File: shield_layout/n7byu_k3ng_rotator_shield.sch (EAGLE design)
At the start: 22 parts, among them J1 ARDUINO_R3_SHIELD

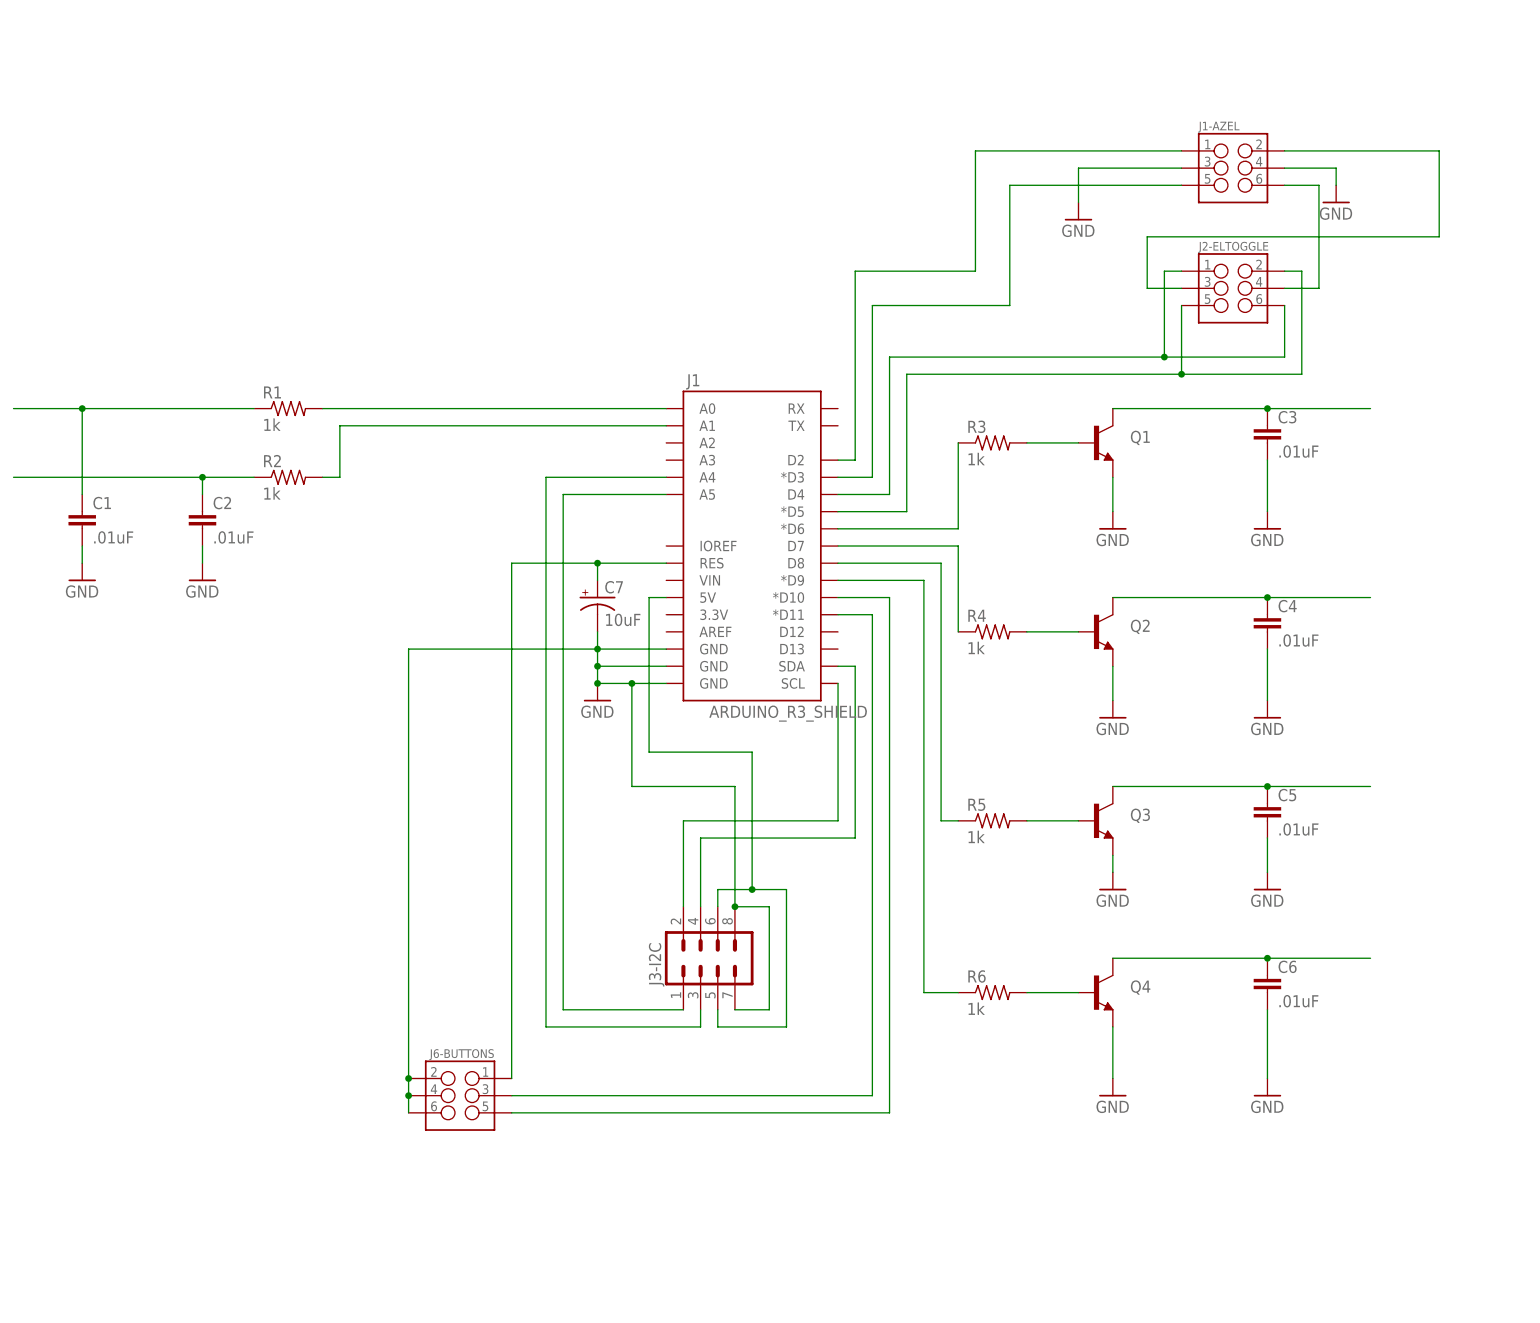
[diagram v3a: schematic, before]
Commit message: switching back to separate headers. hopefully will be easier to route on the PCB
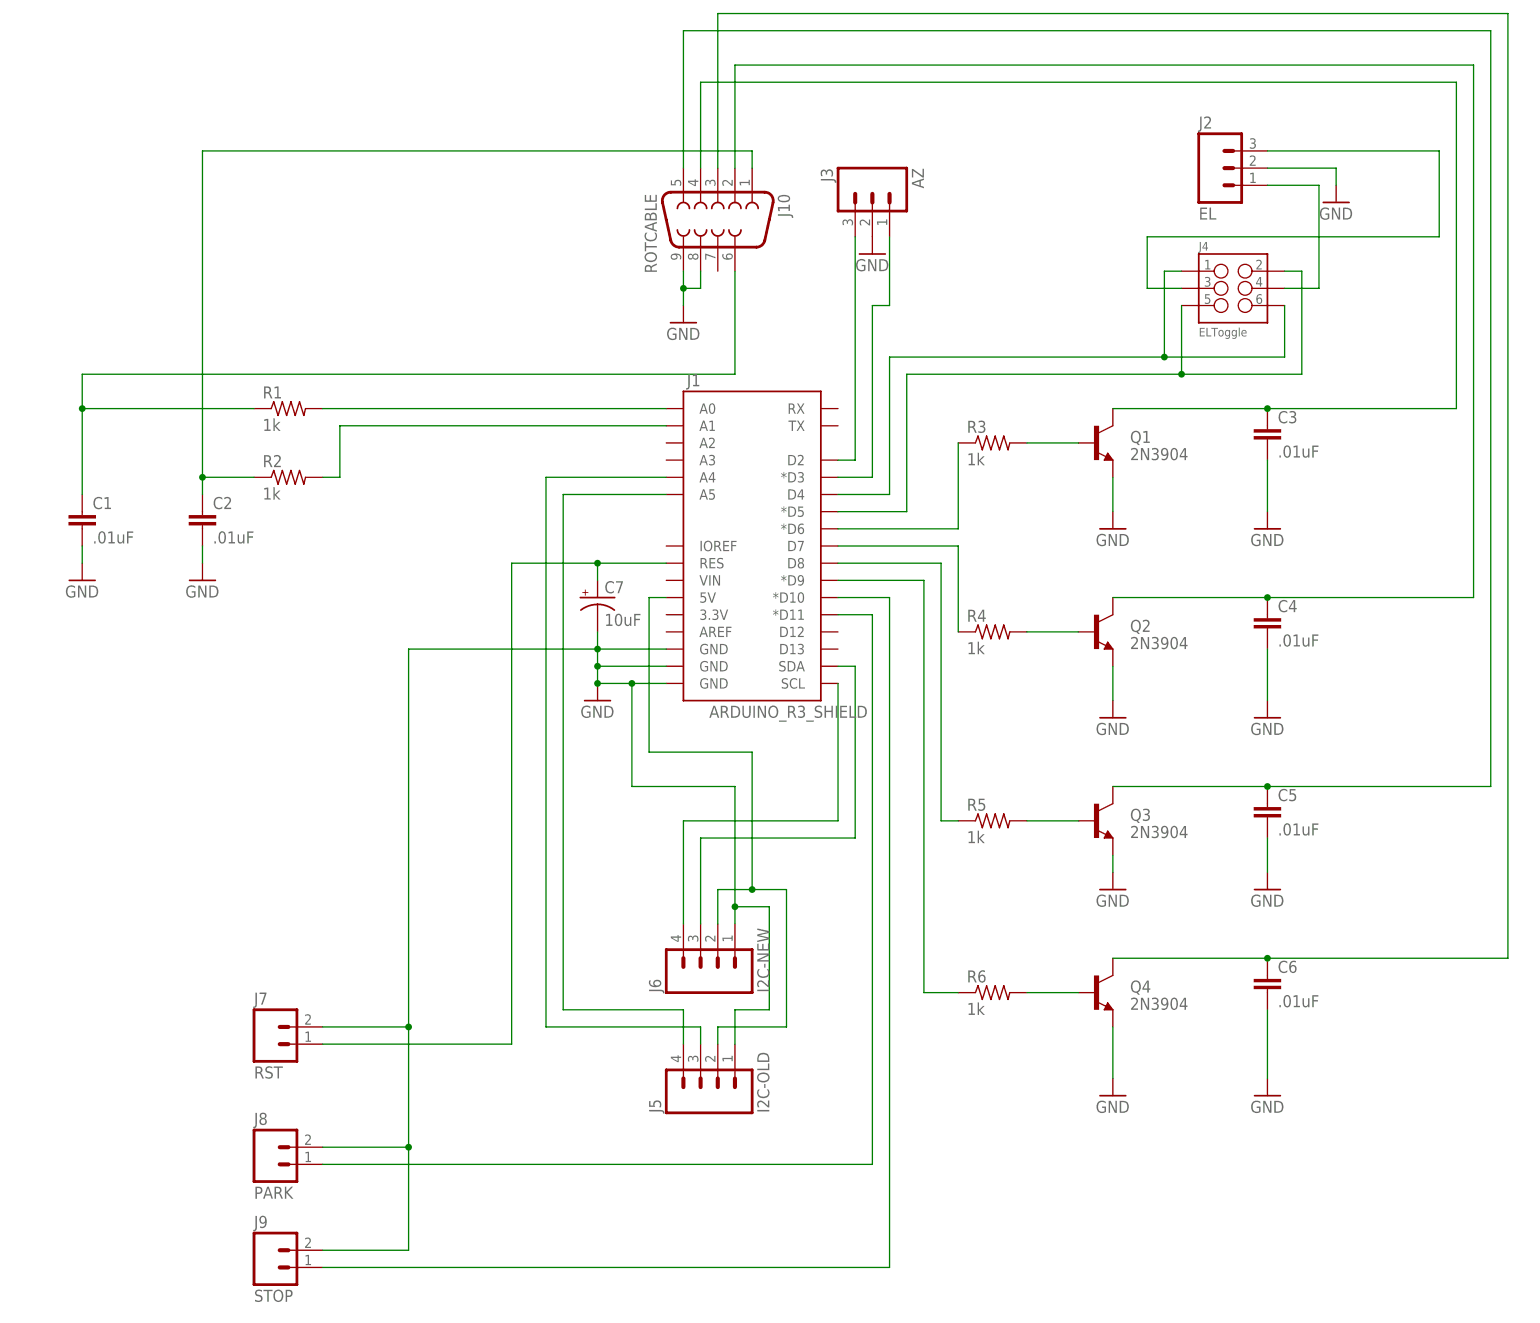
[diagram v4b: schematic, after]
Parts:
- removed J1-AZEL, J6-BUTTONS: (no value), SparkFun-Connectors:M03X22X3_SILK_MALE_PTH
- removed J3-I2C: (no value), SparkFun-Connectors:M04X2
- added J10: ROTCABLE, SparkFun-Connectors:DB9FEMALE
- added J2: EL, SparkFun-Connectors:M03LONGPADS
- added J3: AZ, SparkFun-Connectors:M03LONGPADS
- added J5: I2C-OLD, SparkFun-Connectors:M04LONGPADS
- added J6: I2C-NEW, SparkFun-Connectors:M04LONGPADS
- added J7: RST, SparkFun-Connectors:M02PTH3
- added J8: PARK, SparkFun-Connectors:M02PTH3
- added J9: STOP, SparkFun-Connectors:M02PTH3
- J4: value (none) -> ELToggle
- Q1, Q2, Q3, Q4: value (none) -> 2N3904
- renumbered J2-ELTOGGLE to J4
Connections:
- removed net N$11: C5.1, Q3.C
- new net N$18: C5.1, J10.5, Q3.C
- net CCW-BUTTON: now also J3.1; no longer J1-AZEL.5
- net CW-BUTTON: now also J3.3; no longer J1-AZEL.1
- net GND: now also J10.8, J10.9, J2.2, J3.2, J5.1, J6.1, J7.2, J8.2, J9.2; no longer J1-AZEL.3, J1-AZEL.4, J3-I2C.7, J3-I2C.8, J6-BUTTONS.2, J6-BUTTONS.4, J6-BUTTONS.6
- net N$1: now also J10.6
- net N$10: now also J10.2
- net N$12: now also J10.3
- net N$13: now also J7.1; no longer J6-BUTTONS.1
- net N$14: now also J2.1; no longer J1-AZEL.6
- net N$21: now also J2.3; no longer J1-AZEL.2
- net N$25: now also J5.4; no longer J3-I2C.1
- net N$26: now also J5.2, J6.2; no longer J3-I2C.5, J3-I2C.6
- net N$27: now also J5.3; no longer J3-I2C.3
- net N$28: now also J9.1; no longer J6-BUTTONS.5
- net N$29: now also J6.3; no longer J3-I2C.4
- net N$31: now also J8.1; no longer J6-BUTTONS.3
- net N$32: now also J6.4; no longer J3-I2C.2
- net N$5: now also J10.1
- net N$9: now also J10.4
